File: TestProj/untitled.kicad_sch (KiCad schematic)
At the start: 1 part

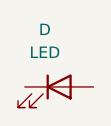
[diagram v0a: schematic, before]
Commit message: added more sheets for demonstration
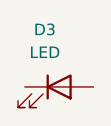
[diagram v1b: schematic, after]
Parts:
- renumbered D to D3
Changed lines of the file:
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@@
 		(dnp no)
 		(fields_autoplaced yes)
-		(property "Reference" "D"
+		(property "Reference" "D?"
 			(at 173.6725 82.55 0)
 			(effects
@@
 					(unit 1)
 				)
+				(path "/c118cc56-38ad-4e47-aa36-07d1c7ff5ecd/6f91e8cb-c44e-4208-b78f-fc922fa94200"
+					(reference "D?")
+					(unit 1)
+				)
